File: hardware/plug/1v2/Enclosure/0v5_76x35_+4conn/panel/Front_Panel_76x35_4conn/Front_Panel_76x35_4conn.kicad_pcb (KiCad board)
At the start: 2 copper layers, 76 x 35 mm, 5 parts

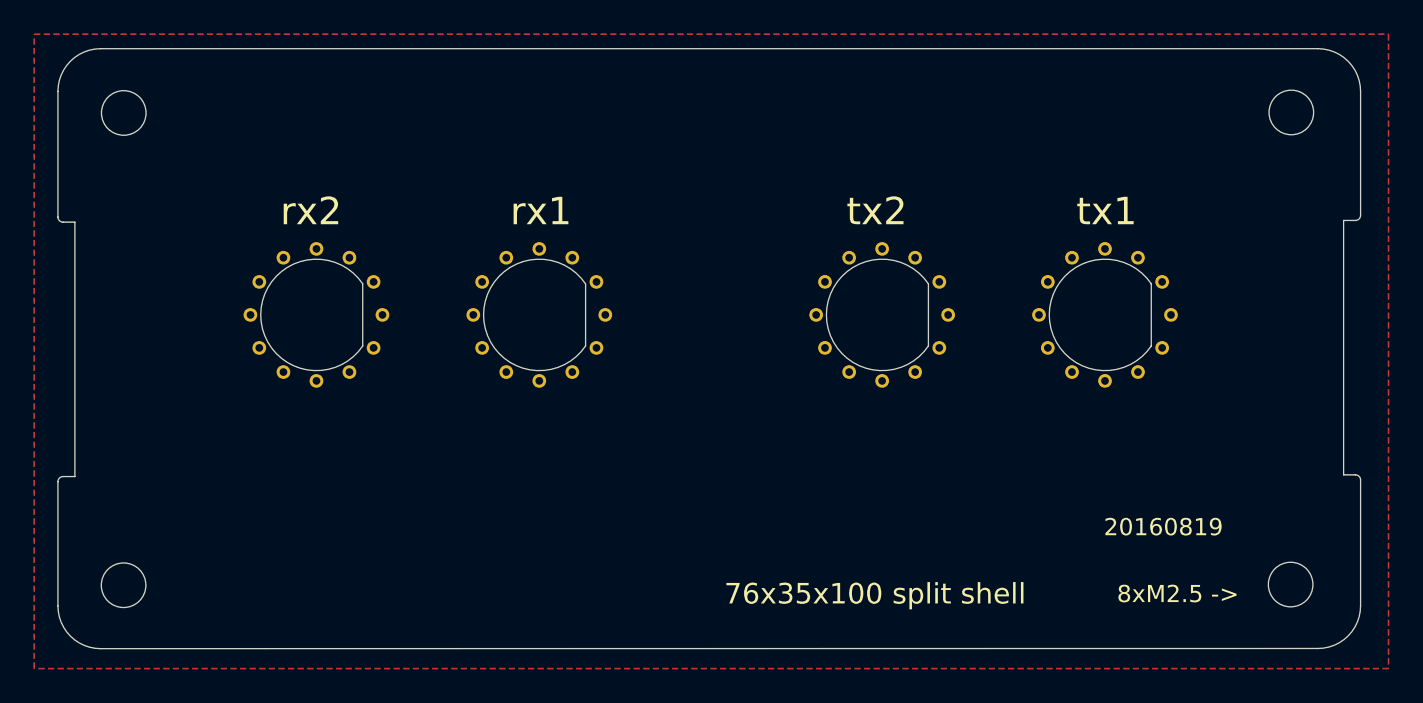
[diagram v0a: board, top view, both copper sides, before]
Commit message: 0v5 version
add 4 connector version
move screw holes according found datasheet, hopefully more accurate
board outline is "improved"
fixes bug #10
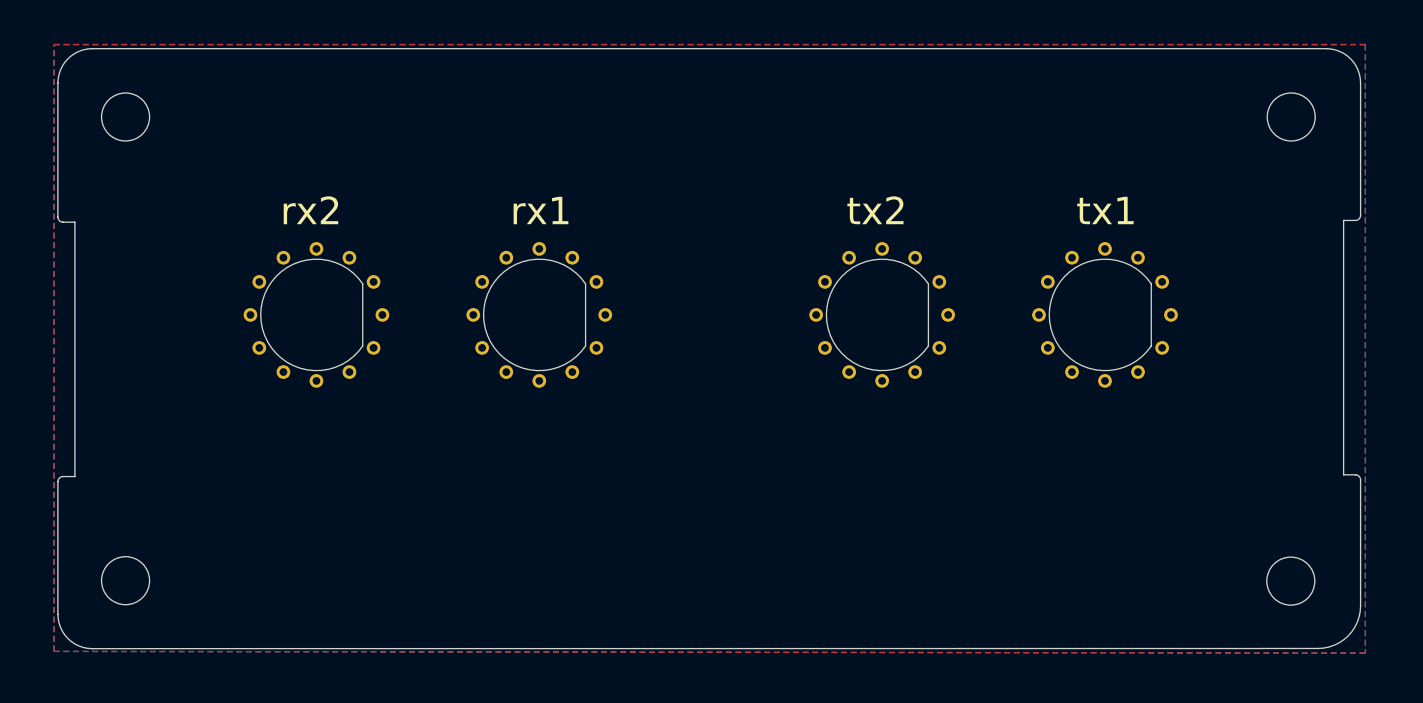
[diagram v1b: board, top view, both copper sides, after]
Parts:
- moved G*** 0.17 mm to (55.8, 124.3), turned to 0 degrees
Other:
- outline, holes or cut-outs redrawn
- board text added: "20160902"
- board text added: "luftek"
- board text removed: "20160819"
- board text removed: "8xM2.5 ->"

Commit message: 3rd batch ready for fab house
Gerber output produced
Combined into a panel

Added small holes on backside for "ventilation" #7
Naming is consistent with current LimeSDR boards W, L, H order for TX #2

Text stays on Silkscreen for now #8
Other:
- board text added: "20160924"
- board text removed: "20160902"
